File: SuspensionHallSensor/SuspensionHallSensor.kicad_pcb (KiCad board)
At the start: 2 copper layers, 12 x 12 mm, 5 parts, among them J1 Conn_01x03_Pin, U1 DRV5055A1xDBZxQ1

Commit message: Added graphics
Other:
- board text added: "Pack Motorsports Baja SAE"
- board text added: "Suspension Hall Sensor Board REV.1"

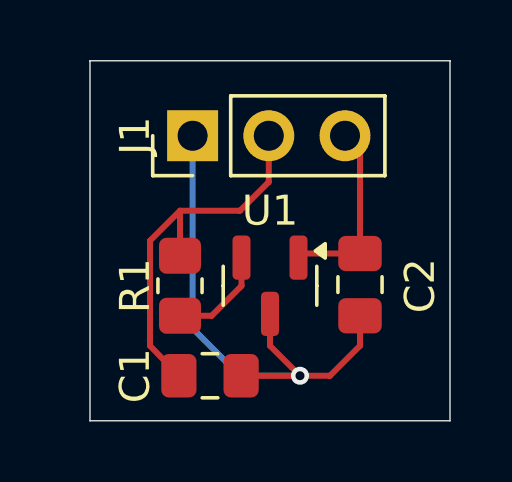
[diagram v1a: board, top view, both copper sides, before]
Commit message: Added pinout graphics
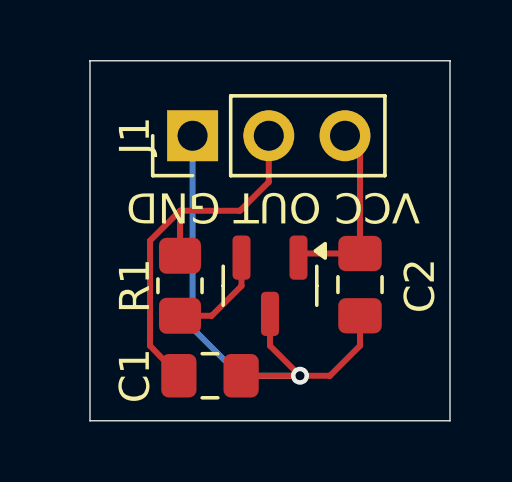
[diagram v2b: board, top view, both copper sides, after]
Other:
- board text added: "VCC OUT GND"
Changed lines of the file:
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@@
 			(at -2.5 0 180)
 			(layer "F.SilkS")
+			(hide yes)
 			(effects
 				(font
@@
 		)
 		(fp_text user "${REFERENCE}"
-			(at 0 2.54 360)
+			(at 0 2.54 0)
 			(layer "F.Fab")
 			(effects
@@
 		)
 	)
+	(gr_text "VCC OUT GND"
+		(at 155.5 99.8 180)
+		(layer "F.SilkS")
+		(effects
+			(font
+				(size 1 1)
+				(thickness 0.1)
+			)
+			(justify left bottom)
+		)
+	)
